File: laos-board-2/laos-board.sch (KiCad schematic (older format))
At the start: 96 parts, among them IC1 KB847, IC2 KB847, J1 USB-A, J10 I2C, J11 MBED NXP, J12 JP, J13 ZEXT, J14 ANALOG, J15 JP, J16 JP_3, J17 POLOLU1201, J18 YAXIS, J19 JP, J2 CAN, J20 YEXT, J21 JP, J22 JP_3, J23 POLOLU1201, J24 XAXIS, J25 JP, J26 XEXT, J27 OUTPUT, J28 VSENSOR, J29 INPUT12, J3 USBPWR, J30 JP, J31 JP_3, J32 POLOLU1201, J33 EAXIS, J34 INPUT34, J35 JP, J36 EEXT, J37 OUTPUT12, J38 VCPU, J39 OUTPUT34, J4 MAGJACK, J40 JP, J5 VMOT, J6 JP, J7 JP_3, J8 POLOLU1201, J9 ZAXIS, Q1 TIP115, Q2 TIP115, U1 65HVD251, U2 SDCARD, U3 7805

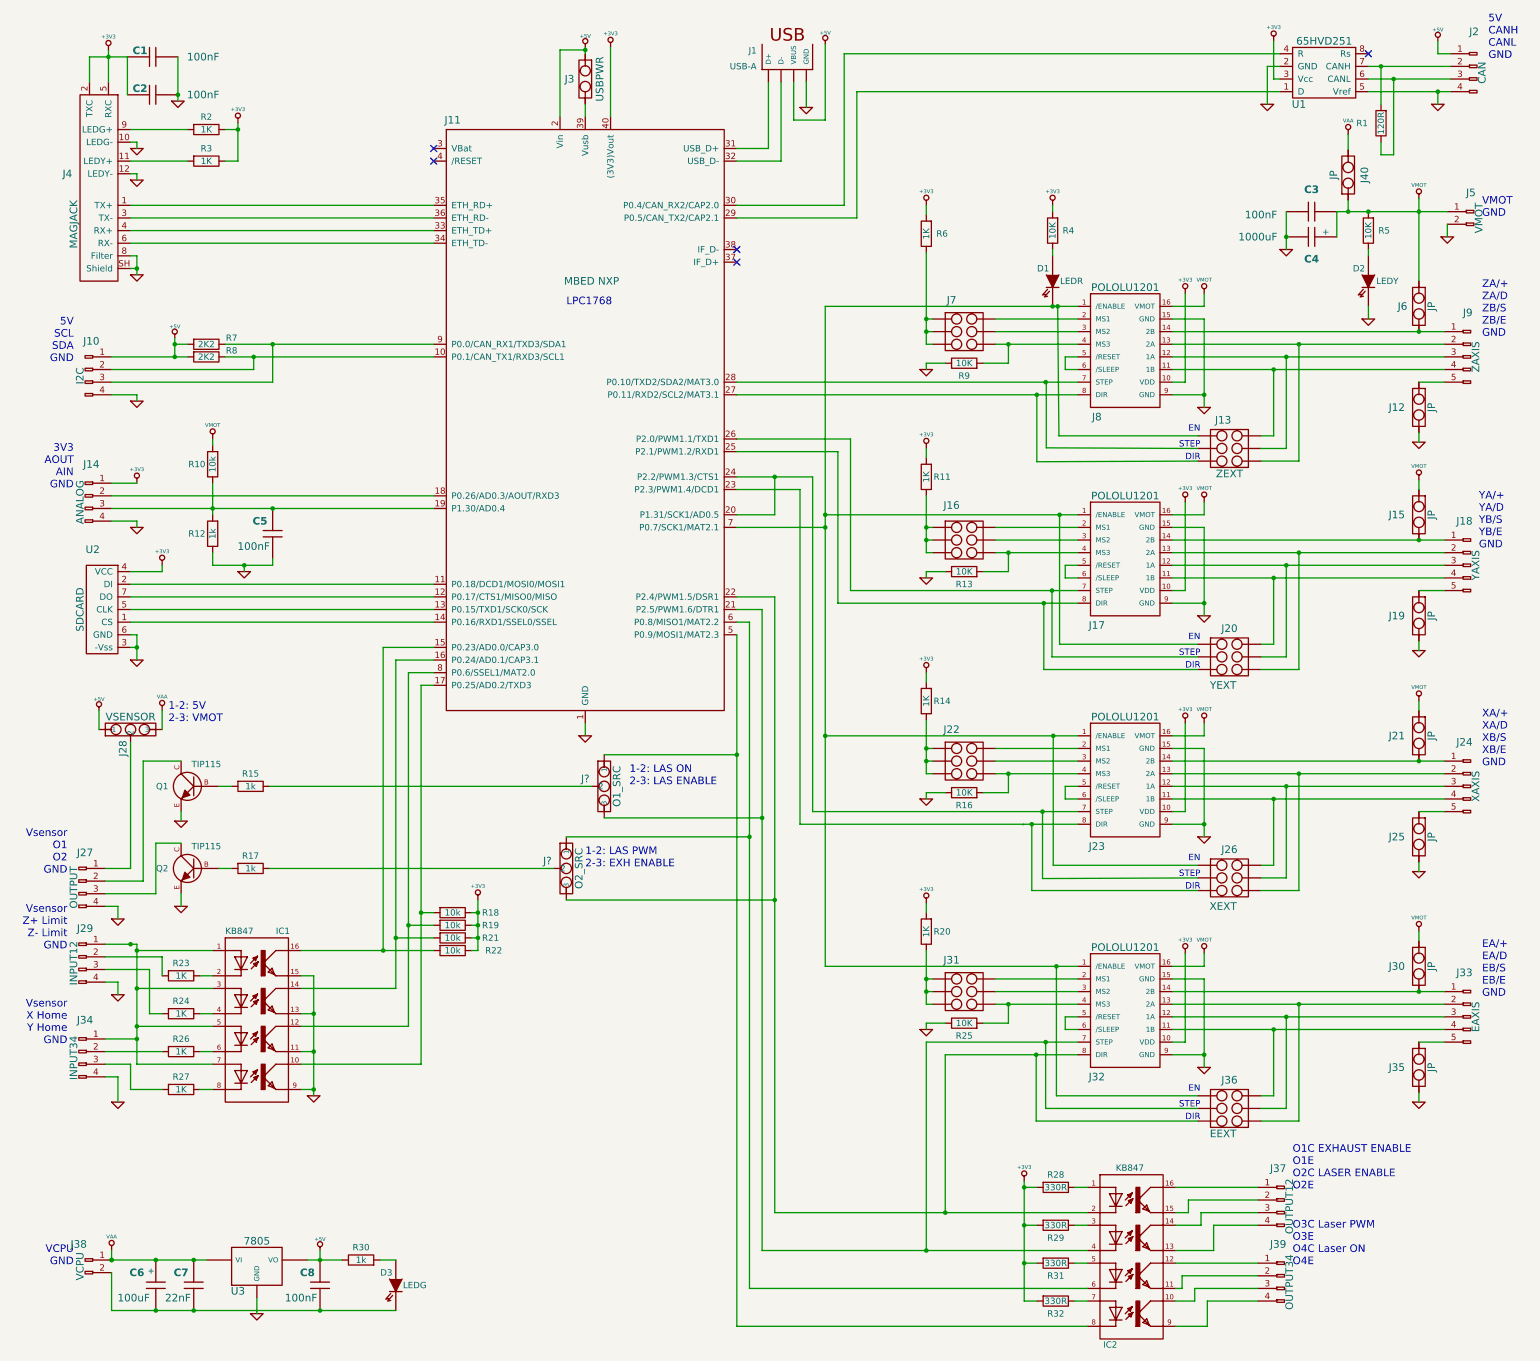
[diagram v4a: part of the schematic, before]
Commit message: Connect forgotten nets and generate new netlist
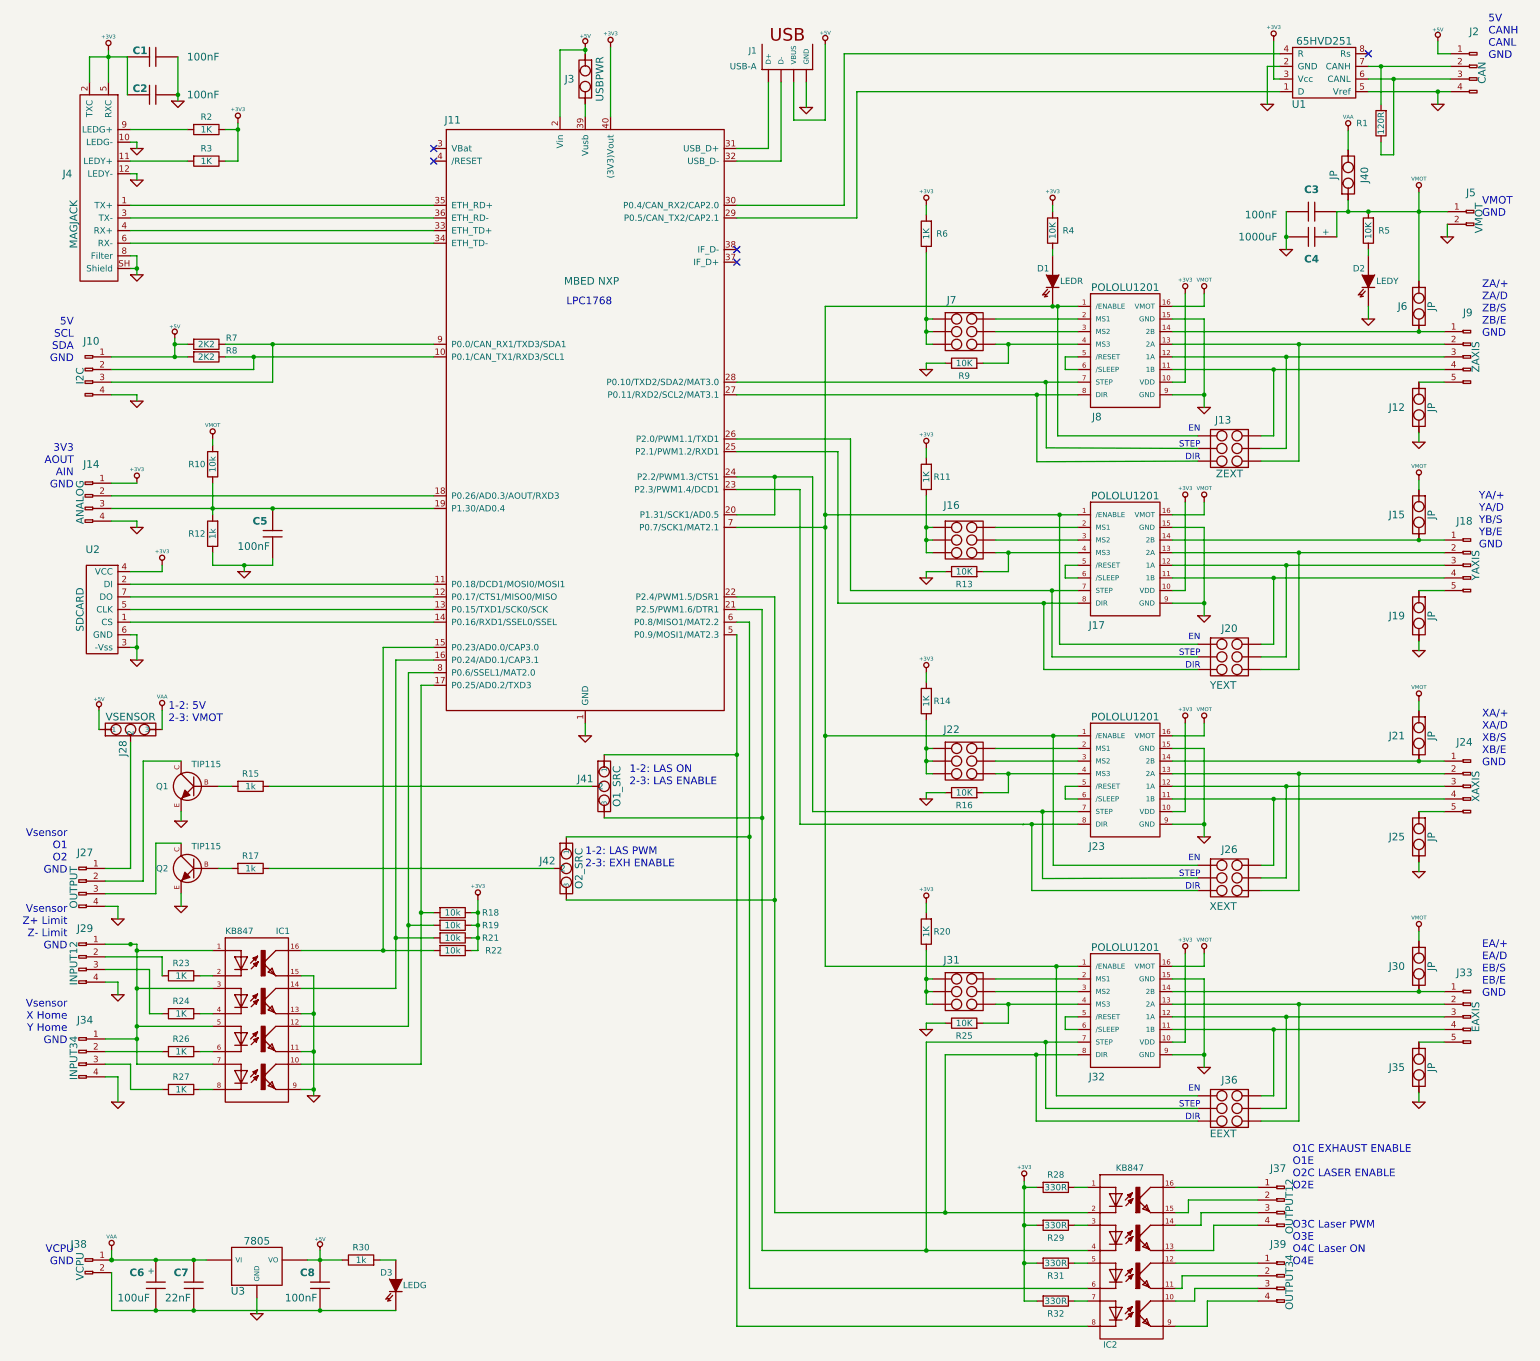
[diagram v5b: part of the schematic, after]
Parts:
- gave numbers to parts that had none: 2
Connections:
- net GND: now also J1.GND
- net at D1.2 (K), J11.7 (P0.7/SCK1/MAT2.1), J17.1 (/ENABLE)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: now also J13.6 (P4)

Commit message: Connect some new nets in the pcb, and some modules, bad ubuntu
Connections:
- net at IC2.2, J11.22 (P2.4/PWM1.5/DSR1), J32.8 (DIR)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: now also J36.1 (P1); no longer J36.5 (P3)
- net at J11.23 (P2.3/PWM1.4/DCD1), J23.8 (DIR): now also J26.1 (P1); no longer J26.5 (P3)
- net at J11.25 (P2.1/PWM1.2/RXD1), J17.8 (DIR): now also J20.1 (P1); no longer J20.5 (P3)
- net at J11.27 (P0.11/RXD2/SCL2/MAT3.1), J8.8 (DIR): now also J13.6 (P4); no longer J13.2 (P6)
- net at D1.2 (K), J11.7 (P0.7/SCK1/MAT2.1), J17.1 (/ENABLE)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: now also J13.2 (P6), J20.5 (P3), J26.5 (P3), J36.5 (P3); no longer J13.6 (P4), J20.1 (P1), J26.1 (P1), J36.1 (P1)
- net at C3.2, C4.1 (+), J40.1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: no longer J6.1

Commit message: more board updates...
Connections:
- net labels added: VMOTO

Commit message: Exchange VMOT for VPP because of weird kicad bug
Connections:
- net labels added: VPP
- net labels removed: VMOT, VMOTO
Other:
- note added: "Note: VPP is VMOTOR, bug in kicad power netlist for now ..."
